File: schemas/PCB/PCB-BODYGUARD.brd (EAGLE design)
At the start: 46 x 58.1 mm, 38 parts, among them IC1 4050D, Q1 CMA-4544PF-W, U1 MAX4466EXK+T, X1 MICROSD

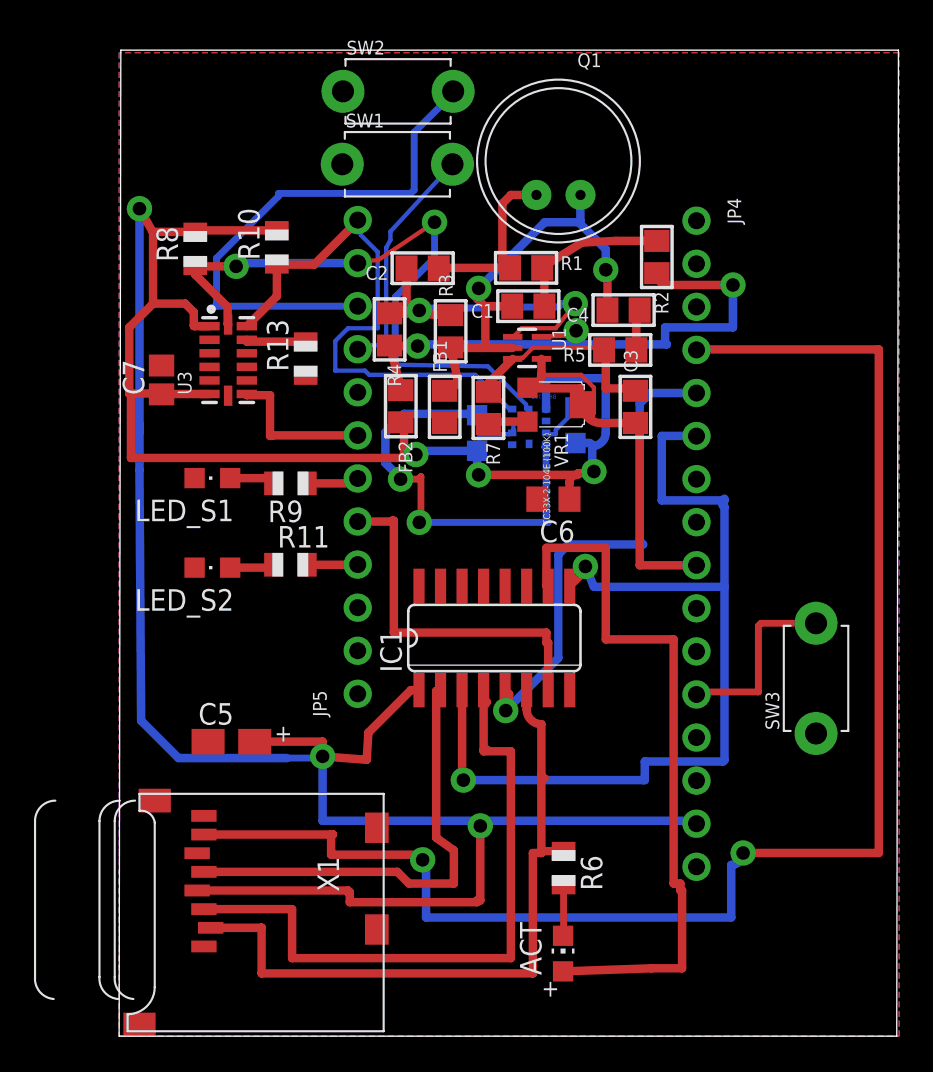
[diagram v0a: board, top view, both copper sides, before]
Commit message: ajout des fichiers PCB
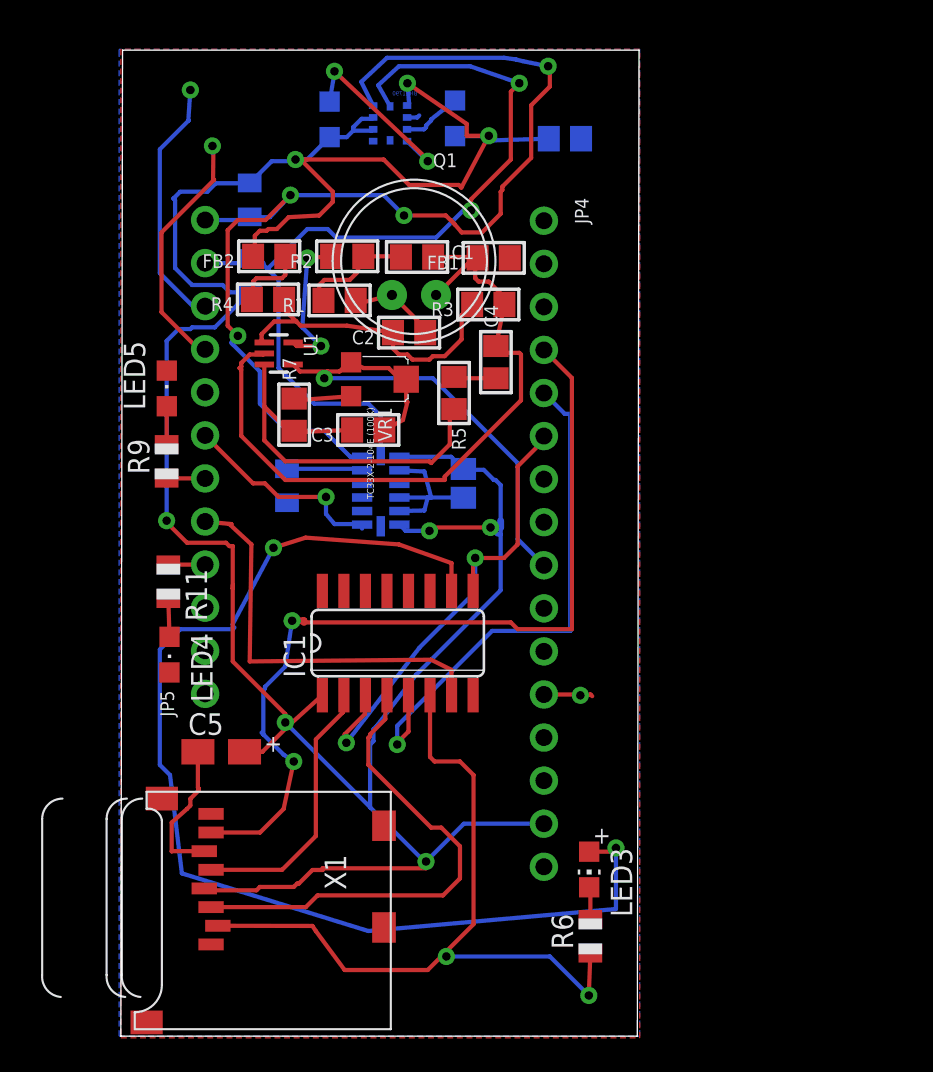
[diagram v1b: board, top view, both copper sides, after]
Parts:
- removed ACT: RED, adafruit:CHIP-LED0805
- removed LED_S1, LED_S2: (no value), adafruit:CHIPLED_0805
- removed SW1, SW2, SW3: (no value), adafruit:TACT_PANA-EVQ
- removed U$31: BH1790, quentin:BH1790
- removed U3: (no value), microbuilder:LGA14
- added ADXL: (no value), microbuilder:LGA14
- added BH1790: BH1790, quentin:BH1790
- added LED3: RED, adafruit:CHIP-LED0805
- added LED4: Red, adafruit:CHIPLED_0805
- added LED5: green, adafruit:CHIPLED_0805
- C5: value 10uF/10V -> 10uF
- C6: value (none) -> 1uF
- LED1, LED2: value (none) -> green
- R11, R9: value 10K -> 1K
- moved C6 21.3 mm to (26.3, 52.9), flipped to the bottom
- moved LED2 20.4 mm to (12.4, 54.1)
- moved LED1 19.4 mm to (19.8, 54.1)
- moved C7 18.8 mm to (20.3, 32.6), flipped to the bottom, turned to 270 degrees
- moved R2 18.3 mm to (13.4, 46.0), turned to 180 degrees
- moved C3 15.8 mm to (14.7, 35.8), turned to 180 degrees
- moved U1 14.7 mm to (9.41, 40.3)
- moved FB2 11.8 mm to (8.85, 46.0), turned to 180 degrees
- moved R7 11.5 mm to (10.3, 36.6), turned to 90 degrees
- moved R1 11.2 mm to (13.0, 43.4), turned to 180 degrees
- moved VR1 10.5 mm to (15.5, 38.7)
- moved Q1 10.4 mm to (17.4, 45.7)
- moved R5 10.1 mm to (19.8, 37.9), turned to 270 degrees
- moved FB1 9.25 mm to (22.1, 45.9), turned to 180 degrees
- moved JP5 9.00 mm to (5.07, 34.2)
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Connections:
- removed net N$15: LED_S1.A, R9.2
- new net N$17: LED4.A, R11.2
- net +3V3: now also ADXL.1, ADXL.6, BH1790.TEST2, BH1790.VCC, BH1790.VCC2; no longer U$31.TEST2, U$31.VCC, U$31.VCC2, U3.1, U3.6
- net A0: no longer SW3.P$2
- net D10: now also ADXL.8; no longer U3.8
- net D13: now also R11.1; no longer R11.2
- net D5: no longer SW2.P$2
- net D6: no longer SW1.P$2
- net GND: now also ADXL.2, ADXL.4, ADXL.5, BH1790.GND, BH1790.TEST1, LED4.C, LED5.C; no longer LED_S1.C, LED_S2.C, SW1.P$1, SW2.P$1, SW3.P$1, U$31.GND, U$31.TEST1, U3.2, U3.4, U3.5
- net INT2: now also ADXL.9; no longer U3.9
- net N$11: now also LED3.C; no longer ACT.C
- net N$14: now also BH1790.LED2; no longer U$31.LED2
- net N$16: now also LED5.A, R9.2; no longer LED_S2.A, R11.1
- net N$6: now also BH1790.LED1; no longer U$31.LED1
- net N$8: now also LED3.A; no longer ACT.A
- net SCL: now also ADXL.14, BH1790.SCL; no longer U$31.SCL, U3.14
- net SDA: now also ADXL.13, BH1790.SDA; no longer U$31.SDA, U3.13
- net SDO/ADDR: now also ADXL.12; no longer U3.12
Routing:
- net MISO: track 88.8 -> 51.5 mm
- net SDA: track 33.1 -> 66.8 mm, vias 0 -> 4
- net SCK: track 57.5 -> 29.3 mm
- net N$8: track 42.2 -> 67.7 mm, vias 0 -> 2
- net AVCC: track 35.0 -> 14.5 mm, vias 3 -> 2
- net GND: track 0.00 -> 18.4 mm
- net D5: track 31.9 -> 15.0 mm
- net AGND: track 27.1 -> 43.6 mm, vias 2 -> 0
- net SCL: track 37.7 -> 52.8 mm
- net N$14: track 25.5 -> 11.2 mm
- net +3V3: track 185.7 -> 171.7 mm, vias 6 -> 8
- net N$1: track 12.6 -> 25.4 mm
- net N$9: track 27.2 -> 16.3 mm
- net N$12: track 39.4 -> 29.4 mm
- net A3: track 23.3 -> 31.9 mm, vias 0 -> 1
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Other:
- board size 46 x 58.1 mm -> 30.6 x 58.1 mm
